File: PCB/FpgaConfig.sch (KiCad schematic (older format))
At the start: 16 parts, among them J5 TSM-105-01-S-DV, U4 S25FL128SAGMFI000, U5 10CL016YE144C8G, X1 SG-5032CAN

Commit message: Cleaned up the schematics
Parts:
- X1: value SG-5032CAN -> X1G0044510011
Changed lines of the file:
@@
 encoding utf-8
 Sheet 18 19
-Title "FPGA configuration"
+Title "Litter Robot 3 - FPGA configuration"
 Date "2021-03-28"
 Rev "A1"
@@
 AR Path="/603F1F4D/60647CC2/60657577" Ref="X1"  Part="1"
 F 0 "X1" H 2594 1946 50  0000 L CNN
-F 1 "SG-5032CAN" H 2594 1855 50  0000 L CNN
+F 1 "X1G0044510011" H 2594 1855 50  0000 L CNN
 F 2 "Oscillator:Oscillator_SMD_SeikoEpson_SG8002CA-4Pin_7.0x5.0mm" H 2950 1550 50  0001 C CNN
 F 3 "https://support.epson.biz/td/api/doc_check.php?dl=brief_SG5032CAN&lang=en" H 2150 1900 50  0001 C CNN

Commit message: Add support for the weight sensor
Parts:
- renumbered C12 to C18, C13 to C19, R42 to R44, R43 to R45, R44 to R46, R45 to R47, R46 to R48, R47 to R49, R48 to R50, U5 to U4, U4 to U5

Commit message: Add support for the hall sensors and dome LED
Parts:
- renumbered C18 to C21, C19 to C22, R44 to R49, R45 to R50, R46 to R51, R47 to R52, R48 to R53, R49 to R54, R50 to R55, U4 to U5, U5 to U6

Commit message: Fix the oscillator footprint
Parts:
- X1: footprint Oscillator:Oscillator_SMD_SeikoEpson_SG8002CA-4Pin_7.0x5.0mm -> Oscillator:Oscillator_SMD_SeikoEpson_SG8002LB-4Pin_5.0x3.2mm
- renumbered C21 to C14, C22 to C15, R50 to R15, R52 to R16, R53 to R17, R54 to R18, R55 to R19, R51 to R20, R49 to R21, U5 to U2, U6 to U3

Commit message: Add a 3D model for the oscillator
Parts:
- X1: footprint Oscillator:Oscillator_SMD_SeikoEpson_SG8002LB-4Pin_5.0x3.2mm -> LitterRobot:Seiko_SG5032CAN
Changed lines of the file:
@@
 F 0 "X1" H 2594 1946 50  0000 L CNN
 F 1 "X1G0044510011" H 2594 1855 50  0000 L CNN
-F 2 "Oscillator:Oscillator_SMD_SeikoEpson_SG8002LB-4Pin_5.0x3.2mm" H 2950 1550 50  0001 C CNN
+F 2 "LitterRobot:Seiko_SG5032CAN" H 2950 1550 50  0001 C CNN
 F 3 "https://support.epson.biz/td/api/doc_check.php?dl=brief_SG5032CAN&lang=en" H 2150 1900 50  0001 C CNN
 F 4 "X1G0044510011" H 2250 1900 50  0001 C CNN "Part_number"

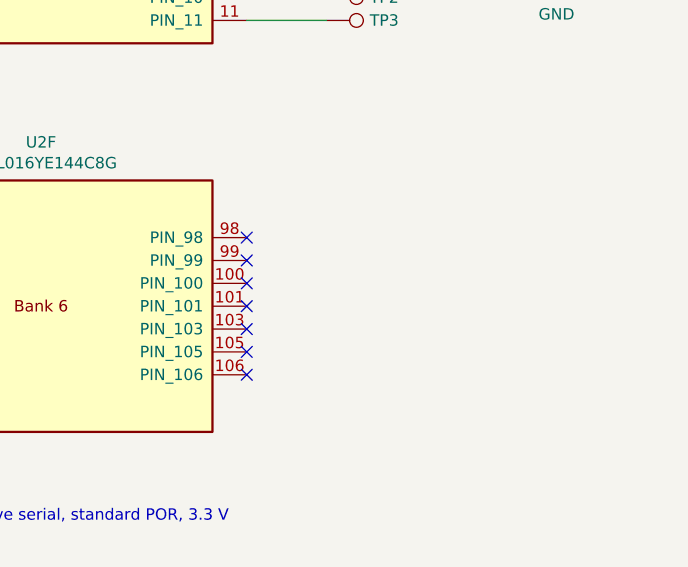
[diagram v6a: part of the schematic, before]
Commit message: Connect the Bluetooth module to the FPGA
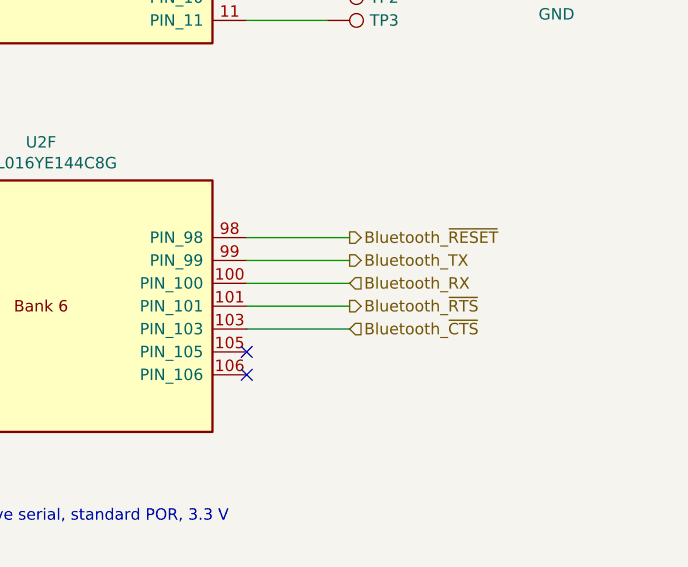
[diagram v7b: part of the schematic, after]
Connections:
- net Bluetooth_RX: now reaches U2.100 (PIN_100)
- net Bluetooth_~RTS: now reaches U2.101 (PIN_101)
- net Bluetooth_~CTS: now reaches U2.103 (PIN_103)
- net Bluetooth_~RESET: now reaches U2.98 (PIN_98)
- net Bluetooth_TX: now reaches U2.99 (PIN_99)
- no-connect marks 14 -> 9
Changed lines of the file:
@@
 NoConn ~ 1750 4700
 NoConn ~ 2750 4600
-NoConn ~ 7150 4250
-NoConn ~ 7150 4350
-NoConn ~ 7150 4450
-NoConn ~ 7150 4550
-NoConn ~ 7150 4650
 NoConn ~ 7150 4750
 NoConn ~ 7150 4850
@@
 Text Notes 750  800  0    50   ~ 0
 Intel® Cyclone® 10 LP Device Family Pin Connection Guidelines:\nhttps://www.intel.com/content/dam/www/programmable/us/en/pdfs/literature/dp/cyclone-10/pcg-01021.pdf
+Text HLabel 7600 4350 2    50   Output ~ 0
+Bluetooth_TX
+Text HLabel 7600 4450 2    50   Input ~ 0
+Bluetooth_RX
+Text HLabel 7600 4650 2    50   Input ~ 0
+Bluetooth_~CTS
+Text HLabel 7600 4550 2    50   Output ~ 0
+Bluetooth_~RTS
+Text HLabel 7600 4250 2    50   Output ~ 0
+Bluetooth_~RESET
+Wire Wire Line
+	7150 4250 7600 4250
+Wire Wire Line
+	7150 4350 7600 4350
+Wire Wire Line
+	7150 4450 7600 4450
+Wire Wire Line
+	7150 4550 7600 4550
+Wire Wire Line
+	7150 4650 7600 4650
 $EndSCHEMATC

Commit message: Route more signals
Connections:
- net Bluetooth_RX: now also U2.103 (PIN_103); no longer U2.100 (PIN_100)
- net Bluetooth_~CTS: now also U2.101 (PIN_101); no longer U2.103 (PIN_103)
- net Bluetooth_~RTS: now also U2.100 (PIN_100); no longer U2.101 (PIN_101)
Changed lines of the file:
@@
 Text Notes 750  800  0    50   ~ 0
 Intel® Cyclone® 10 LP Device Family Pin Connection Guidelines:\nhttps://www.intel.com/content/dam/www/programmable/us/en/pdfs/literature/dp/cyclone-10/pcg-01021.pdf
-Text HLabel 7600 4350 2    50   Output ~ 0
-Bluetooth_TX
-Text HLabel 7600 4450 2    50   Input ~ 0
-Bluetooth_RX
-Text HLabel 7600 4650 2    50   Input ~ 0
-Bluetooth_~CTS
-Text HLabel 7600 4550 2    50   Output ~ 0
-Bluetooth_~RTS
 Text HLabel 7600 4250 2    50   Output ~ 0
 Bluetooth_~RESET
@@
 Wire Wire Line
 	7150 4650 7600 4650
+Text HLabel 7600 4350 2    50   Output ~ 0
+Bluetooth_TX
+Text HLabel 7600 4450 2    50   Output ~ 0
+Bluetooth_~RTS
+Text HLabel 7600 4650 2    50   Input ~ 0
+Bluetooth_RX
+Text HLabel 7600 4550 2    50   Input ~ 0
+Bluetooth_~CTS
 $EndSCHEMATC
